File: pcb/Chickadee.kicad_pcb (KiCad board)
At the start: 2 copper layers, 34.5 x 67.2 mm, 37 parts, among them J1 SMA, P1 FTDI, P2 CONN_01X02, P3 CONN_01X01, Q1 Q_NMOS_GSD, Q2 Q_NMOS_GSD, SW1 SW_PUSH, U1 ESP-12E, U2 74LVC1G3157, U3 LM2674M-3.3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

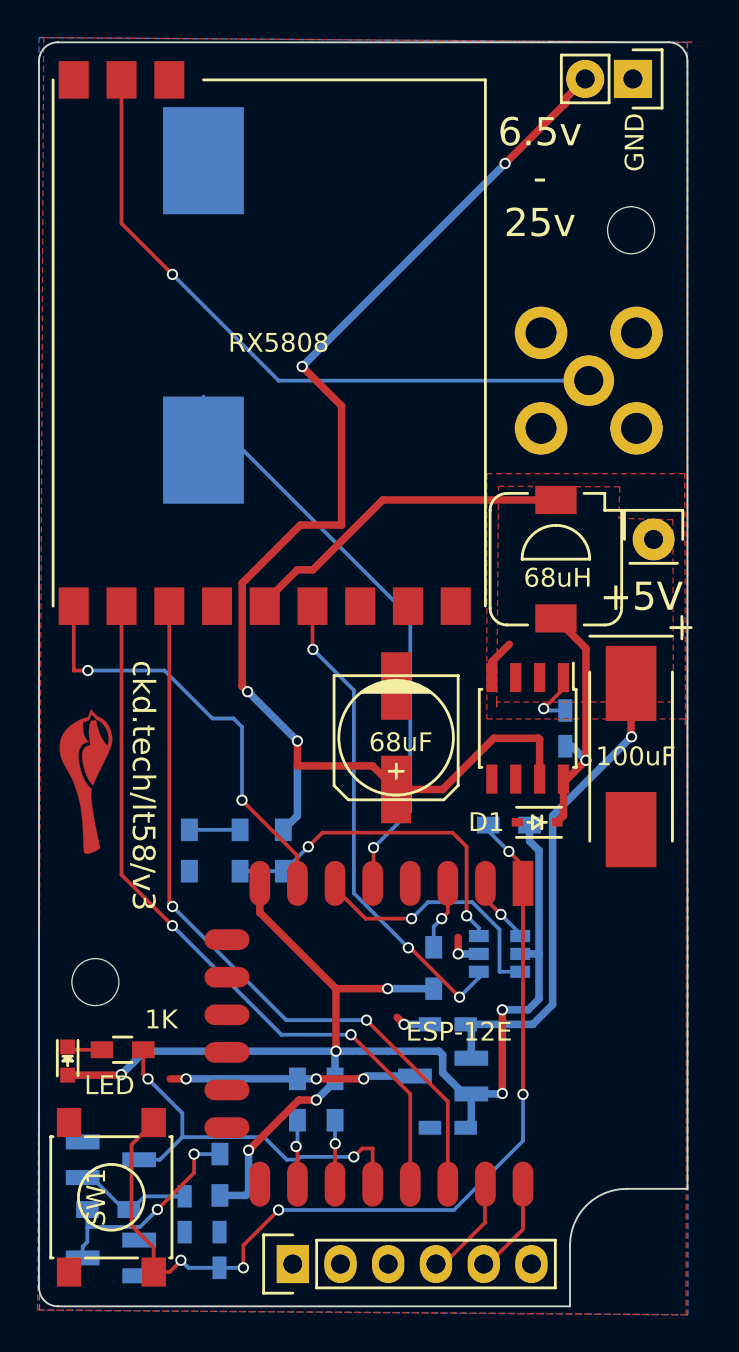
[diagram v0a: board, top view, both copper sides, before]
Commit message: v4 of laptimer with everything connected and RSSI voltage divider.
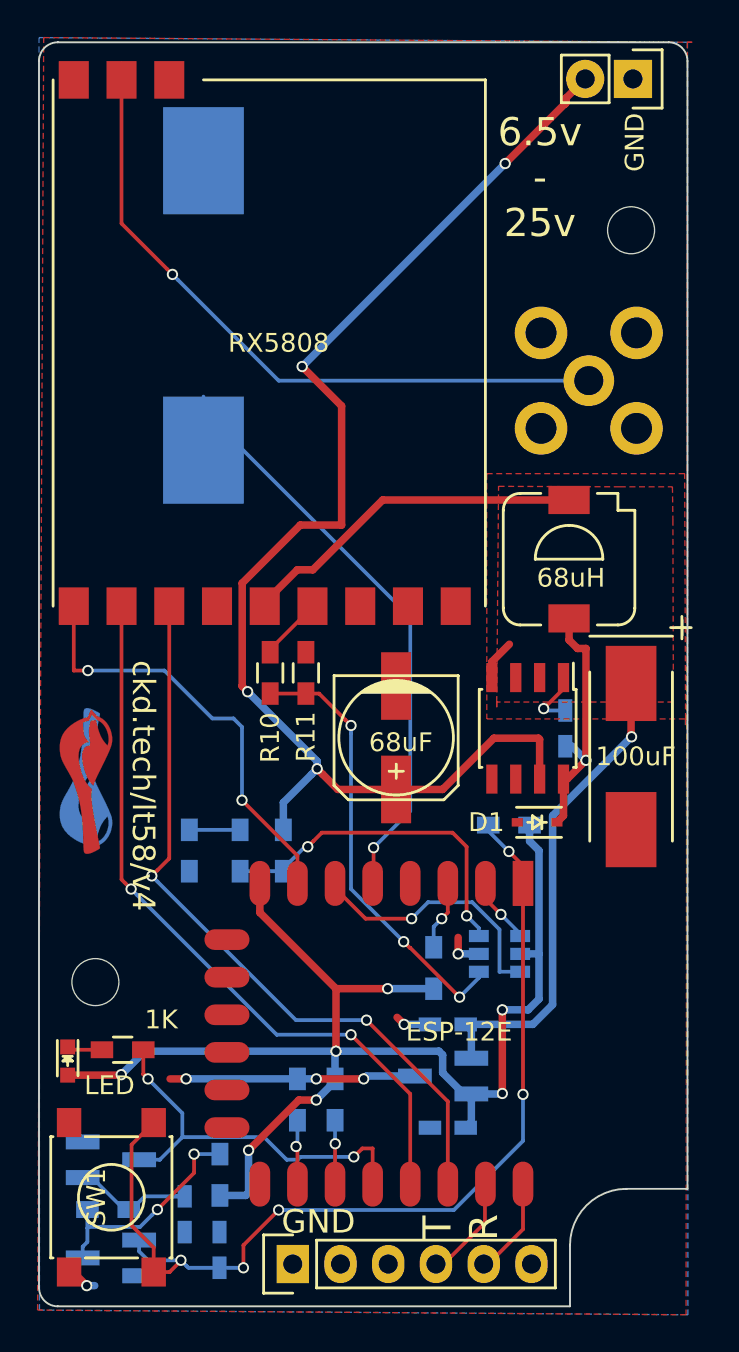
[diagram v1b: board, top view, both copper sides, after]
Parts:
- removed P3: CONN_01X01, Pin_Headers:Pin_Header_Straight_1x01
- added G***: Chickadee 3mm, chickadee_logo:chickadee_3mm_fcu, B.Cu at (182.5, 101.5)
- added R10: 1k, Resistors_SMD:R_0603_HandSoldering, F.Cu at (192.3, 95.8)
- added R11: 10k, Resistors_SMD:R_0603_HandSoldering, F.Cu at (194.2, 95.8)
- oR1: renamed from Optional Reset Pullup
- moved L1 0.70 mm to (208.2, 89.8)
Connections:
- U2 pad 1: /RSSI -> Net-(R10-Pad2)
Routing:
- net Net-(R10-Pad2): track 0.00 -> 23.6 mm, vias 0 -> 3
- net /RSSI: track 25.9 -> 3.38 mm, vias 3 -> 0
- net /ESP-Reset/RESET: track 50.1 -> 53.1 mm
- net GNDPWR: track 17.0 -> 18.6 mm, vias 5 -> 6
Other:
- board text added: "R"
- board text added: "T"
- board text added: "ckd.tech/lt58/v4"
- board text removed: "+5V"
- board text removed: "ckd.tech/lt58/v3"
